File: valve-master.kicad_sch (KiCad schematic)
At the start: 4 parts, among them J10 VALVE1, J9 VALVE1, U78 DRV8872DDARQ1, U79 DRV8872DDARQ1

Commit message: lots and lots and lots of work
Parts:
- added C108, C109, C110, C111, C118: 0.1uF, symbol Device:C
- added C99: C, symbol Device:C
- added D5: 1N4148, symbol Device:D
- added J17, J18, J19, J20, J21, J22, J23, J24, J25, J26, J27, J28: VALVE, symbol Connector:Conn_01x02_Socket
- added Q9: DMN3007LSSQ, Package_SO:SOIC-8_3.9x4.9mm_P1.27mm, symbol Transistor_FET:IRF8721PBF-1
- added R108: R, symbol Device:R
- added R109: 100, symbol Device:R
- added R110, R201: 10K, symbol Device:R
- added U100, U101, U102, U103, U93, U94, U95, U96, U97, U98, U99: DRV8872DDARQ1, Package_SO:Texas_HTSOP-8-1EP_3.9x4.9mm_P1.27mm_EP2.95x4.9mm_Mask2.4x3.1mm_ThermalVias, symbol Driver_Motor:DRV8872DDA
- added U104, U105, U107, U108: SN74HCS595-Q1, femta-control:DHVQFN-16-2.5X3.5MM, symbol 74xx:74HC595
- added U106: SN74LVC2G125, Package_SO:VSSOP-8_2.4x2.1mm_P0.5mm, symbol femta-control-custom:SN74LVC2G125DCU-Q1
- J10, J9: value VALVE1 -> VALVE
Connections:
- net +12V: now also D5.1 (K), J28.1 (Pin_1), U100.5 (VM), U101.5 (VM), U102.5 (VM), U103.5 (VM), U93.5 (VM), U94.5 (VM), U95.5 (VM), U96.5 (VM), U97.5 (VM), U98.5 (VM), U99.5 (VM)
- net CLOSE_FEMTA1: now also U104.1 (QB)
- net CLOSE_FEMTA2: now also U104.3 (QD)
- net GND: now also C108.2, C109.2, C110.2, C111.2, C118.2, Q9.1 (S), Q9.2 (S), Q9.3 (S), R110.2, U100.1 (GND), U100.7 (ISEN), U100.9 (GND), U101.1 (GND), U101.7 (ISEN), U101.9 (GND), U102.1 (GND), U102.7 (ISEN), U102.9 (GND), U103.1 (GND), U103.7 (ISEN), U103.9 (GND), U104.8 (GND), U105.8 (GND), U106.4 (GND), U107.8 (GND), U108.8 (GND), U93.1 (GND), U93.7 (ISEN), U93.9 (GND), U94.1 (GND), U94.7 (ISEN), U94.9 (GND), U95.1 (GND), U95.7 (ISEN), U95.9 (GND), U96.1 (GND), U96.7 (ISEN), U96.9 (GND), U97.1 (GND), U97.7 (ISEN), U97.9 (GND), U98.1 (GND), U98.7 (ISEN), U98.9 (GND), U99.1 (GND), U99.7 (ISEN), U99.9 (GND)
- net OPEN_FEMTA1: now also U104.15 (QA)
- net OPEN_FEMTA2: now also U104.2 (QC)
- new net: J22.2 (Pin_2), U98.6 (OUT1)
- new net: J22.1 (Pin_1), U98.8 (OUT2)
- new net: J26.2 (Pin_2), U102.6 (OUT1)
- new net: J26.1 (Pin_1), U102.8 (OUT2)
- new net: C99.1, D5.2 (A), J28.2 (Pin_2), R108.2
- new net: J17.1 (Pin_1), U93.8 (OUT2)
- new net: J17.2 (Pin_2), U93.6 (OUT1)
- new net: J20.2 (Pin_2), U96.6 (OUT1)
- new net: J20.1 (Pin_1), U96.8 (OUT2)
- new net: C99.2, Q9.5 (D), Q9.6 (D), Q9.7 (D), Q9.8 (D), R108.1
- new net: J21.2 (Pin_2), U97.6 (OUT1)
- new net: J21.1 (Pin_1), U97.8 (OUT2)
- new net: J24.2 (Pin_2), U100.6 (OUT1)
- new net: J24.1 (Pin_1), U100.8 (OUT2)
- new net: U107.9 (QH'), U108.14 (SER)
- new net: J25.2 (Pin_2), U101.6 (OUT1)
- new net: J25.1 (Pin_1), U101.8 (OUT2)
- new net: U105.9 (QH'), U107.14 (SER)
- new net: J18.2 (Pin_2), U94.6 (OUT1)
- new net: J18.1 (Pin_1), U94.8 (OUT2)
- new net: Q9.4 (G), R109.2
- new net: J23.2 (Pin_2), U99.6 (OUT1)
- new net: J23.1 (Pin_1), U99.8 (OUT2)
- new net: U104.9 (QH'), U105.14 (SER)
- new net: J27.2 (Pin_2), U103.6 (OUT1)
- new net: J27.1 (Pin_1), U103.8 (OUT2)
- new net: J19.1 (Pin_1), U95.8 (OUT2)
- new net: J19.2 (Pin_2), U95.6 (OUT1)
- new net +3.3V: C108.1, C109.1, C110.1, C111.1, C118.1, U104.10 (~{SRCLR}), U104.16 (VCC), U105.10 (~{SRCLR}), U105.16 (VCC), U106.8 (VCC), U107.10 (~{SRCLR}), U107.16 (VCC), U108.10 (~{SRCLR}), U108.16 (VCC)
- new net +5V: R201.1
- new net 595_CLK: U104.11 (SRCLK), U105.11 (SRCLK), U106.6 (1Y), U107.11 (SRCLK), U108.11 (SRCLK)
- new net 595_CS: U106.1 (1~{OE}), U106.7 (2~{OE})
- new net 595_DATA: U104.14 (SER), U106.3 (2Y)
- new net CLOSE_FEMTA10: U100.2 (IN2), U107.3 (QD)
- new net CLOSE_FEMTA11: U101.2 (IN2), U107.5 (QF)
- new net CLOSE_FEMTA12: U102.2 (IN2), U107.7 (QH)
- new net CLOSE_FEMTA3: U104.5 (QF), U93.2 (IN2)
- new net CLOSE_FEMTA4: U104.7 (QH), U94.2 (IN2)
- new net CLOSE_FEMTA5: U105.1 (QB), U95.2 (IN2)
- new net CLOSE_FEMTA6: U105.3 (QD), U96.2 (IN2)
- new net CLOSE_FEMTA7: U105.5 (QF), U97.2 (IN2)
- new net CLOSE_FEMTA8: U105.7 (QH), U98.2 (IN2)
- new net CLOSE_FEMTA9: U107.1 (QB), U99.2 (IN2)
- new net EN_OUTPUTS: R201.2, U104.13 (~{OE}), U105.13 (~{OE}), U107.13 (~{OE}), U108.13 (~{OE})
- new net LOAD_OUTPUTS: U104.12 (RCLK), U105.12 (RCLK), U107.12 (RCLK), U108.12 (RCLK)
- new net OPEN_FEMTA10: U100.3 (IN1), U107.2 (QC)
- new net OPEN_FEMTA11: U101.3 (IN1), U107.4 (QE)
- new net OPEN_FEMTA12: U102.3 (IN1), U107.6 (QG)
- new net OPEN_FEMTA3: U104.4 (QE), U93.3 (IN1)
- new net OPEN_FEMTA4: U104.6 (QG), U94.3 (IN1)
- new net OPEN_FEMTA5: U105.15 (QA), U95.3 (IN1)
- new net OPEN_FEMTA6: U105.2 (QC), U96.3 (IN1)
- new net OPEN_FEMTA7: U105.4 (QE), U97.3 (IN1)
- new net OPEN_FEMTA8: U105.6 (QG), U98.3 (IN1)
- new net OPEN_FEMTA9: U107.15 (QA), U99.3 (IN1)
- new net SPI_CLK: U106.2 (1A)
- new net SPI_MOSI: U106.5 (2A)
- new net TANK_FILL_BYPASS: U103.2 (IN2), U108.1 (QB)
- new net TANK_FILL_OPEN: U103.3 (IN1), U108.15 (QA)
- new net TANK_ISO_OPEN: R109.1, R110.1, U108.2 (QC)
- no-connect marks 2 -> 19

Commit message: 540 COMPONENTS I AM LOSING MY MINDDDDDD
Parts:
- renumbered C110 to C58, C108 to C59, C99 to C60, C109 to C61, C111 to C62, C118 to C63, J20 to J10, J24 to J11, J28 to J12, J17 to J13, J21 to J14, J25 to J15, J18 to J16, J22 to J17, J26 to J18, J19 to J5, J23 to J6, J27 to J7, J9 to J8, J10 to J9, Q9 to Q18, R201 to R106, R110 to R107, R109 to R108, R108 to R109, U95 to U49, U99 to U50, U103 to U51, U79 to U52, U106 to U53, U78 to U54, U96 to U55, U100 to U56, U104 to U57, U93 to U58, U97 to U59, U101 to U60, U105 to U61, U94 to U62, U98 to U63, U102 to U64, U107 to U65, U108 to U66
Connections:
- net +5V is gone; now on net +3.3V: R106.1
- net EN_OUTPUTS renamed EN_OUT_595
- net LOAD_OUTPUTS renamed LOAD_595

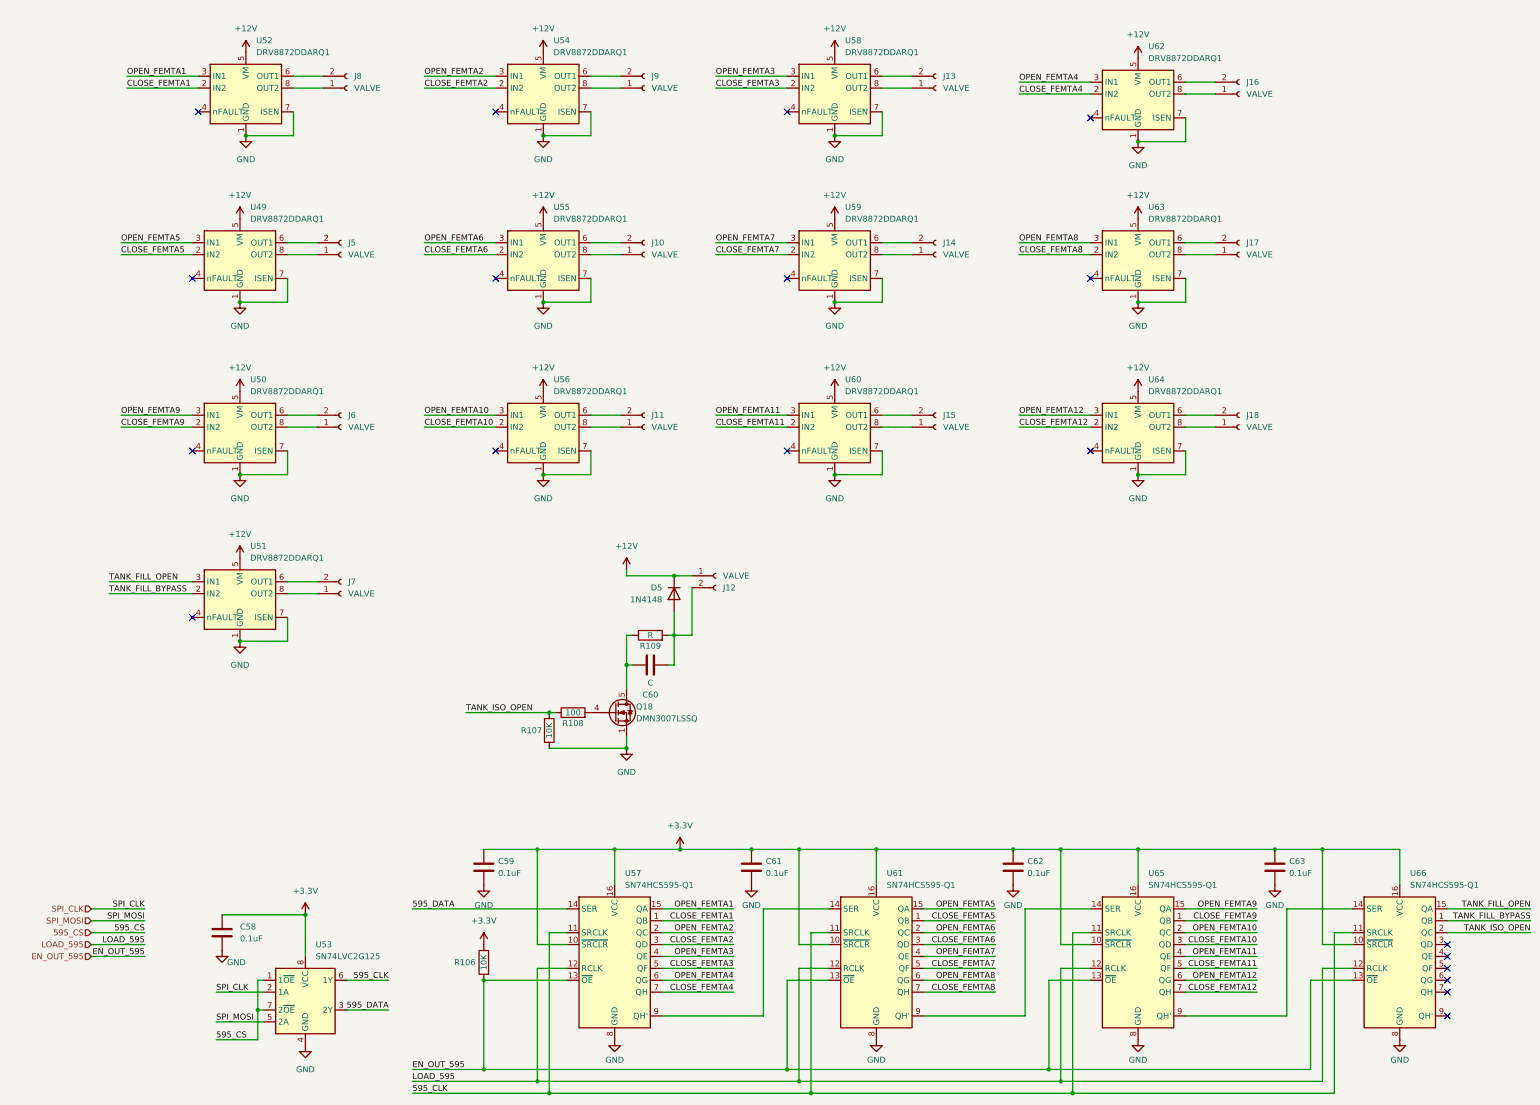
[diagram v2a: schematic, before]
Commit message: page sizes
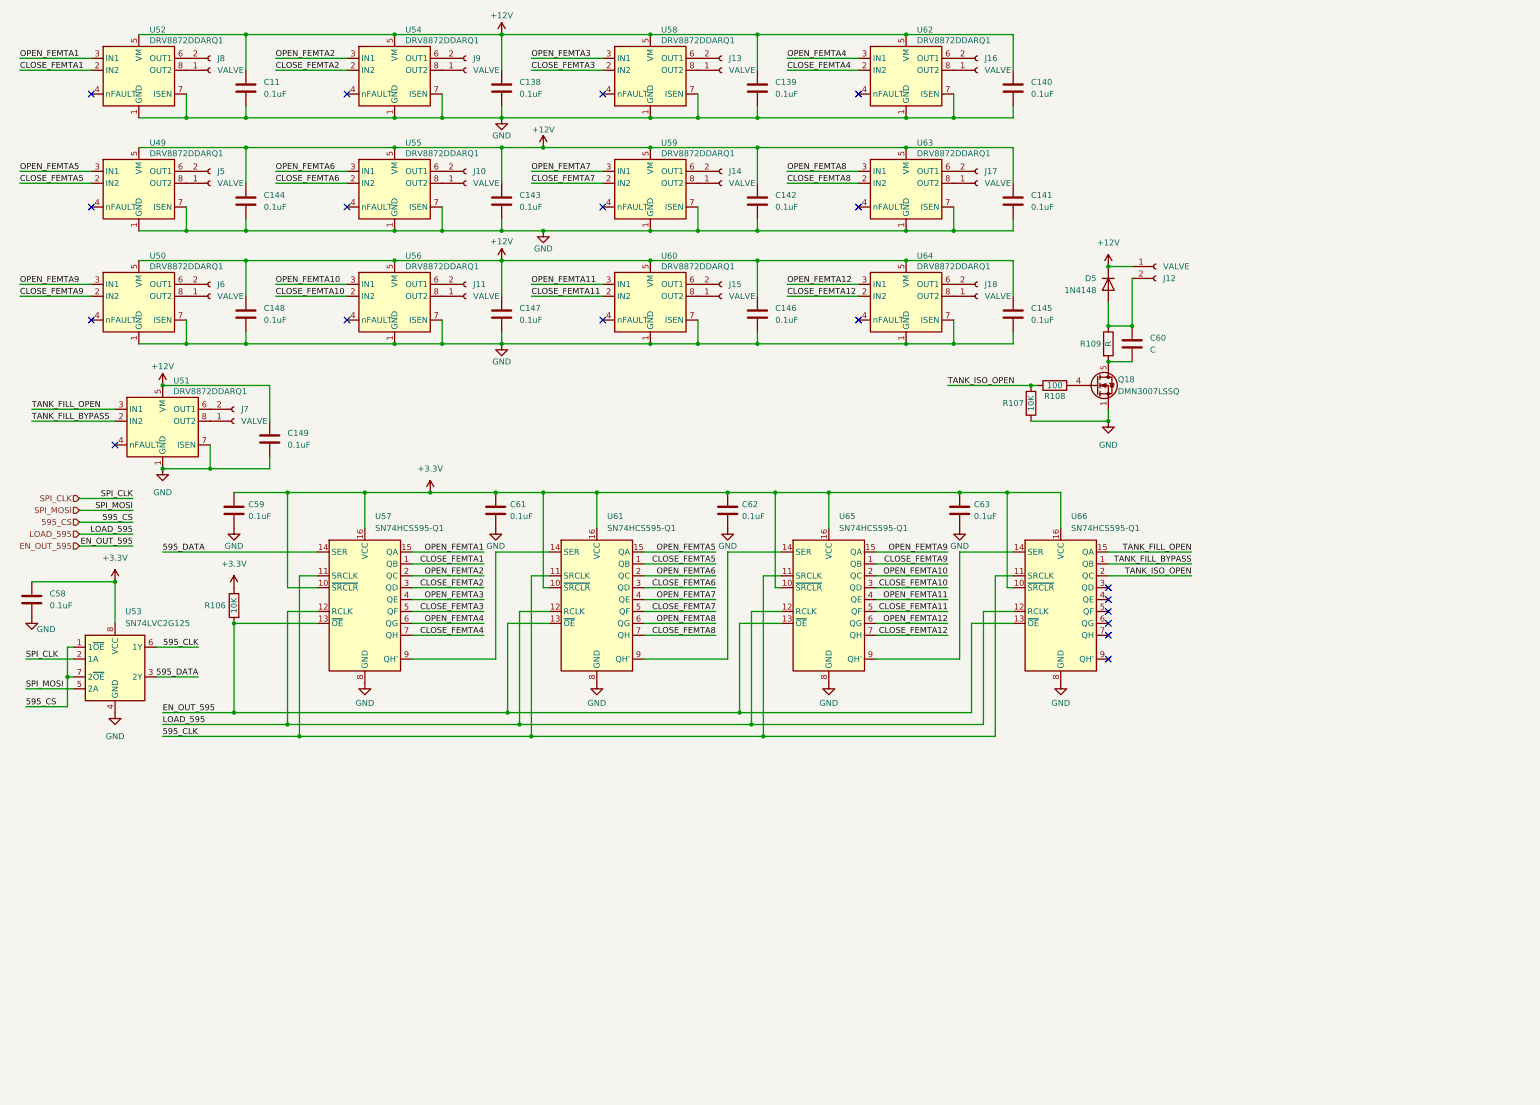
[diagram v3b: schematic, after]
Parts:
- added C11, C138, C139, C140, C141, C142, C143, C144, C145, C146, C147, C148, C149: 0.1uF, symbol Device:C
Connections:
- net +12V: now also C11.1, C138.1, C139.1, C140.1, C141.1, C142.1, C143.1, C144.1, C145.1, C146.1, C147.1, C148.1, C149.1
- net GND: now also C11.2, C138.2, C139.2, C140.2, C141.2, C142.2, C143.2, C144.2, C145.2, C146.2, C147.2, C148.2, C149.2
- net at C60.1, D5.2 (A), J12.2 (Pin_2): now also R109.1; no longer R109.2
- net at C60.2, Q18.5 (D), Q18.6 (D)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: now also R109.2; no longer R109.1
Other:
- moved on the sheet: C58, C59, C61, C62, C63, D5, J10, J11, J12, J13, J14, J15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

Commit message: schematic finished milestone
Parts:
- renumbered C58 to C62, C59 to C63, C11 to C64, C144 to C65, C148 to C66, C149 to C67, C61 to C68, C138 to C69, C143 to C70, C147 to C71, C62 to C72, C139 to C73, C142 to C74, C146 to C75, C63 to C76, C140 to C77, C141 to C78, C145 to C79, C60 to C80, D5 to D6, J13 to J12, J14 to J13, J15 to J14, J16 to J15, J17 to J16, J18 to J17, J12 to J18, J8 to J5, J5 to J6, J6 to J7, J7 to J8, R106 to R115, R107 to R116, R108 to R117, R109 to R118, U53 to U49, U52 to U50, U49 to U51, U50 to U52, U51 to U53, U57 to U54, U54 to U55, U55 to U56, U56 to U57, U61 to U58, U58 to U59, U59 to U60, U60 to U61, U65 to U62, U62 to U63, U63 to U64, U64 to U65

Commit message: RC values
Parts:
- removed C80: C, symbol Device:C
- added C80: 470uF, symbol Device:C_Polarized
- R118: value R -> 98
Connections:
- net at D6.2 (A), J18.2 (Pin_2), R118.1: now also C80.1
- net at Q18.5 (D), Q18.6 (D), Q18.7 (D)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: now also C80.2
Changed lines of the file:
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@@
 	)
 	(junction
+		(at 251.46 82.55)
+		(diameter 0)
+		(color 0 0 0 0)
+	)
+	(junction
 		(at 203.2 44.45)
 		(diameter 0)
@@
 	)
 	(junction
-		(at 251.46 82.55)
-		(diameter 0)
-		(color 0 0 0 0)
-	)
-	(junction
 		(at 118.11 165.1)
 		(diameter 0)
@@
 	)
 	(symbol
-		(lib_id "Device:C")
-		(at 251.46 86.36 0)
+		(lib_id "power:GND")
+		(at 44.45 113.03 0)
 		(unit 1)
 		(exclude_from_sim no)
@@
 		(dnp no)
 		(fields_autoplaced yes)
-		(property "Reference" "C80"
-			(at 255.27 85.0899 0)
+		(property "Reference" "#PWR0169"
+			(at 44.45 119.38 0)
 			(effects
 				(font
 					(size 1.27 1.27)
 				)
-				(justify left)
+				(hide yes)
 			)
 		)
-		(property "Value" "C"
-			(at 255.27 87.6299 0)
+		(property "Value" "GND"
+			(at 44.45 118.11 0)
 			(effects
 				(font
 					(size 1.27 1.27)
 				)
-				(justify left)
 			)
 		)
 		(property "Footprint" ""
-			(at 252.4252 90.17 0)
+			(at 44.45 113.03 0)
 			(effects
 				(font
@@
 			)
 		)
-		(property "Datasheet" "~"
-			(at 251.46 86.36 0)
+		(property "Datasheet" ""
+			(at 44.45 113.03 0)
 			(effects
 				(font
@@
 			)
 		)
-		(property "Description" "Unpolarized capacitor"
-			(at 251.46 86.36 0)
+		(property "Description" "Power symbol creates a global label with name \"GND\" , ground"
+			(at 44.45 113.03 0)
 			(effects
 				(font
@@
 			)
 		)
-		(pin "2"
-		)
 		(pin "1"
 		)
@@
 			(project "femta-control"
 				(path "/838bf11c-36b7-41d7-9462-fe98a188d617/1a97e3f3-1996-4f2f-9833-0a2e3ec261dd"
-					(reference "C80")
+					(reference "#PWR0169")
 					(unit 1)
 				)
@@
 	)
 	(symbol
-		(lib_id "power:GND")
-		(at 44.45 113.03 0)
+		(lib_id "Device:C_Polarized")
+		(at 251.46 86.36 0)
 		(unit 1)
 		(exclude_from_sim no)
@@
 		(dnp no)
 		(fields_autoplaced yes)
-		(property "Reference" "#PWR0169"
-			(at 44.45 119.38 0)
+		(property "Reference" "C80"
+			(at 255.27 84.2009 0)
 			(effects
 				(font
 					(size 1.27 1.27)
 				)
-				(hide yes)
+				(justify left)
 			)
 		)
-		(property "Value" "GND"
-			(at 44.45 118.11 0)
+		(property "Value" "470uF"
+			(at 255.27 86.7409 0)
 			(effects
 				(font
 					(size 1.27 1.27)
 				)
+				(justify left)
 			)
 		)
 		(property "Footprint" ""
-			(at 44.45 113.03 0)
+			(at 252.4252 90.17 0)
 			(effects
 				(font
@@
 			)
 		)
-		(property "Datasheet" ""
-			(at 44.45 113.03 0)
+		(property "Datasheet" "~"
+			(at 251.46 86.36 0)
 			(effects
 				(font
@@
 			)
 		)
-		(property "Description" "Power symbol creates a global label with name \"GND\" , ground"
-			(at 44.45 113.03 0)
+		(property "Description" "Polarized capacitor"
+			(at 251.46 86.36 0)
 			(effects
 				(font
@@
 		(pin "1"
 		)
+		(pin "2"
+		)
 		(instances
 			(project "femta-control"
 				(path "/838bf11c-36b7-41d7-9462-fe98a188d617/1a97e3f3-1996-4f2f-9833-0a2e3ec261dd"
-					(reference "#PWR0169")
+					(reference "C80")
 					(unit 1)
 				)
@@
 			)
 		)
-		(property "Value" "R"
+		(property "Value" "98"
 			(at 246.38 86.36 90)
 			(effects

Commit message: capacitor footprints
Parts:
- C62, C63, C64, C65, C66, C67, C68, C69, C70, C71, C72, C73, C74, C75, C76, C77, C78, C79: footprint (none) -> Capacitor_SMD:C_0603_1608Metric
- C80: footprint (none) -> femta-control:Vishay 597D-H
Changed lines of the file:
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@@
 			)
 		)
-		(property "Footprint" ""
+		(property "Footprint" "Capacitor_SMD:C_0603_1608Metric"
 			(at 63.1952 83.82 0)
 			(effects
@@
 			)
 		)
-		(property "Footprint" ""
+		(property "Footprint" "Capacitor_SMD:C_0603_1608Metric"
 			(at 116.5352 125.73 0)
 			(effects
@@
 			)
 		)
-		(property "Footprint" ""
+		(property "Footprint" "femta-control:Vishay 597D-H"
 			(at 252.4252 90.17 0)
 			(effects
@@
 			)
 		)
-		(property "Footprint" ""
+		(property "Footprint" "Capacitor_SMD:C_0603_1608Metric"
 			(at 117.8052 35.56 0)
 			(effects
@@
 			)
 		)
-		(property "Footprint" ""
+		(property "Footprint" "Capacitor_SMD:C_0603_1608Metric"
 			(at 215.5952 125.73 0)
 			(effects
@@
 			)
 		)
-		(property "Footprint" ""
+		(property "Footprint" "Capacitor_SMD:C_0603_1608Metric"
 			(at 63.1952 59.69 0)
 			(effects
@@
 			)
 		)
-		(property "Footprint" ""
+		(property "Footprint" "Capacitor_SMD:C_0603_1608Metric"
 			(at 117.8052 59.69 0)
 			(effects
@@
 			)
 		)
-		(property "Footprint" ""
+		(property "Footprint" "Capacitor_SMD:C_0603_1608Metric"
 			(at 166.0652 125.73 0)
 			(effects
@@
 			)
 		)
-		(property "Footprint" ""
+		(property "Footprint" "Capacitor_SMD:C_0603_1608Metric"
 			(at 172.4152 59.69 0)
 			(effects
@@
 			)
 		)
-		(property "Footprint" ""
+		(property "Footprint" "Capacitor_SMD:C_0603_1608Metric"
 			(at 17.4752 144.78 0)
 			(effects
@@
 			)
 		)
-		(property "Footprint" ""
+		(property "Footprint" "Capacitor_SMD:C_0603_1608Metric"
 			(at 172.4152 83.82 0)
 			(effects
@@
 			)
 		)
-		(property "Footprint" ""
+		(property "Footprint" "Capacitor_SMD:C_0603_1608Metric"
 			(at 227.0252 59.69 0)
 			(effects
@@
 			)
 		)
-		(property "Footprint" ""
+		(property "Footprint" "Capacitor_SMD:C_0603_1608Metric"
 			(at 60.6552 125.73 0)
 			(effects
@@
 			)
 		)
-		(property "Footprint" ""
+		(property "Footprint" "Capacitor_SMD:C_0603_1608Metric"
 			(at 172.4152 35.56 0)
 			(effects
@@
 			)
 		)
-		(property "Footprint" ""
+		(property "Footprint" "Capacitor_SMD:C_0603_1608Metric"
 			(at 63.1952 35.56 0)
 			(effects
@@
 			)
 		)
-		(property "Footprint" ""
+		(property "Footprint" "Capacitor_SMD:C_0603_1608Metric"
 			(at 68.2752 110.49 0)
 			(effects
@@
 			)
 		)
-		(property "Footprint" ""
+		(property "Footprint" "Capacitor_SMD:C_0603_1608Metric"
 			(at 117.8052 83.82 0)
 			(effects
@@
 			)
 		)
-		(property "Footprint" ""
+		(property "Footprint" "Capacitor_SMD:C_0603_1608Metric"
 			(at 227.0252 35.56 0)
 			(effects
@@
 			)
 		)
-		(property "Footprint" ""
+		(property "Footprint" "Capacitor_SMD:C_0603_1608Metric"
 			(at 227.0252 83.82 0)
 			(effects

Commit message: add more footprints
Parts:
- D6: footprint (none) -> Diode_SMD:D_SOD-123
- R115, R116, R117: footprint (none) -> Resistor_SMD:R_0603_1608Metric
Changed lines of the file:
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@@
 			)
 		)
-		(property "Footprint" ""
+		(property "Footprint" "Diode_SMD:D_SOD-123"
 			(at 246.38 73.66 0)
 			(effects
@@
 			)
 		)
-		(property "Footprint" ""
+		(property "Footprint" "Resistor_SMD:R_0603_1608Metric"
 			(at 61.468 142.24 90)
 			(effects
@@
 			)
 		)
-		(property "Footprint" ""
+		(property "Footprint" "Resistor_SMD:R_0603_1608Metric"
 			(at 234.95 97.028 90)
 			(effects
@@
 			)
 		)
-		(property "Footprint" ""
+		(property "Footprint" "Resistor_SMD:R_0603_1608Metric"
 			(at 228.092 99.06 90)
 			(effects

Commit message: footprint selection
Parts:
- R118: value 98 -> 100; footprint (none) -> Resistor_SMD:R_1206_3216Metric
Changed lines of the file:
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@@
 			)
 		)
-		(property "Value" "98"
+		(property "Value" "100"
 			(at 246.38 86.36 90)
 			(effects
@@
 			)
 		)
-		(property "Footprint" ""
+		(property "Footprint" "Resistor_SMD:R_1206_3216Metric"
 			(at 244.602 86.36 90)
 			(effects
